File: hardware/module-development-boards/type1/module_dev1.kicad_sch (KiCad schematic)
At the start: 34 parts, among them J1 SensorHub_Module_CONN_V1, J10 Conn_01x04, J11 Conn_01x04, J12 Conn_01x01, J13 Conn_01x01, J14 Conn_01x01, J15 Conn_01x01, J16 Conn_01x01, J17 Conn_01x01, J18 Conn_01x01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

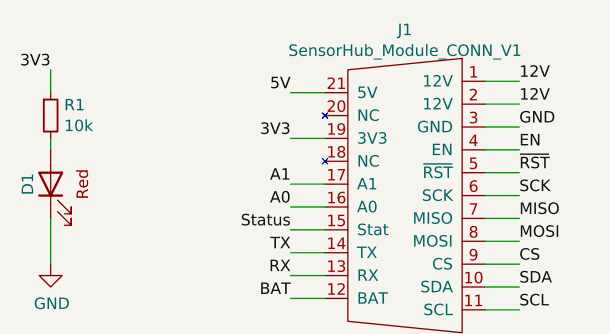
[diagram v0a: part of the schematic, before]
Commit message: cleanup dev board type 1
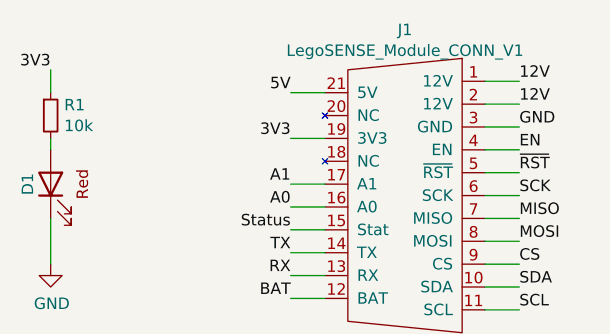
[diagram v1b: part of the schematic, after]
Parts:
- J1: value SensorHub_Module_CONN_V1 -> LegoSENSE_Module_CONN_V1; symbol ICSL:SensorHub_Module_CONN_V1 -> ICSL:LegoSENSE_Module_CONN_V1
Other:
- title: SensorHub Module Development Board -> LegoSENSE Module Development Board
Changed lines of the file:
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@@
   (paper "USLetter")
   (title_block
-    (title "SensorHub Module Development Board")
+    (title "LegoSENSE Module Development Board")
     (date "2021-10-12")
     (rev "V1.0")
@@
     (pin "1")
   )
-  (symbol (lib_id "ICSL:SensorHub_Module_CONN_V1") (at 242.57 31.75 0) (unit 1)
+  (symbol (lib_id "ICSL:LegoSENSE_Module_CONN_V1") (at 242.57 31.75 0) (unit 1)
     (in_bom yes) (on_board yes)
     (property "Reference" "J1" (id 0) (at 242.57 15.875 0))
-    (property "Value" "SensorHub_Module_CONN_V1" (id 1) (at 242.57 18.1864 0))
+    (property "Value" "LegoSENSE_Module_CONN_V1" (id 1) (at 242.57 18.1864 0))
     (property "Footprint" "ICSL:Amphenol_91911-31321LF_PLUG" (id 2) (at 242.57 31.75 0)
       (effects (font (size 1.27 1.27)) hide)
@@
     )
     (path "/00000000-0000-0000-0000-0000608870b5"
-      (reference "J1") (unit 1) (value "SensorHub_Module_CONN_V1") (footprint "ICSL:Amphenol_91911-31321LF_PLUG")
+      (reference "J1") (unit 1) (value "LegoSENSE_Module_CONN_V1") (footprint "ICSL:Amphenol_91911-31321LF_PLUG")
     )
     (path "/00000000-0000-0000-0000-00006168bf3e"
